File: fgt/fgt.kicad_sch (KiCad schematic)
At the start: 28 parts, among them J1 Conn_01x03, J2 USB_B_Mini, J4 Conn_01x06, SW1 Reset, SW2 SW-, SW3 SW_M/BOOT, SW4 SW+, U1 ESP32-C3-WROOM-02, U3 BMP280, U4 HT75xx-1-SOT89

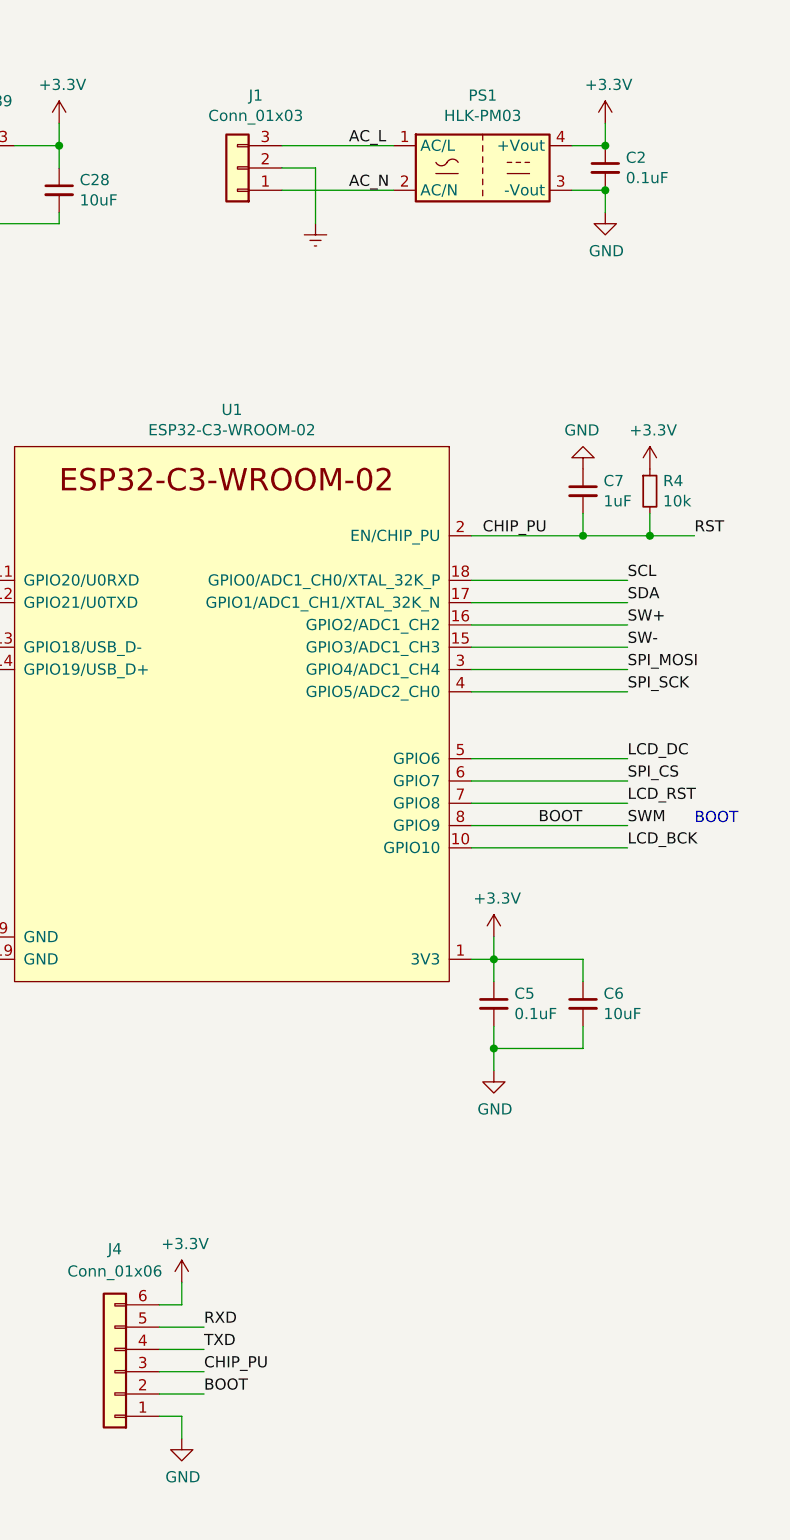
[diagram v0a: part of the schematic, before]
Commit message: placing locating holes
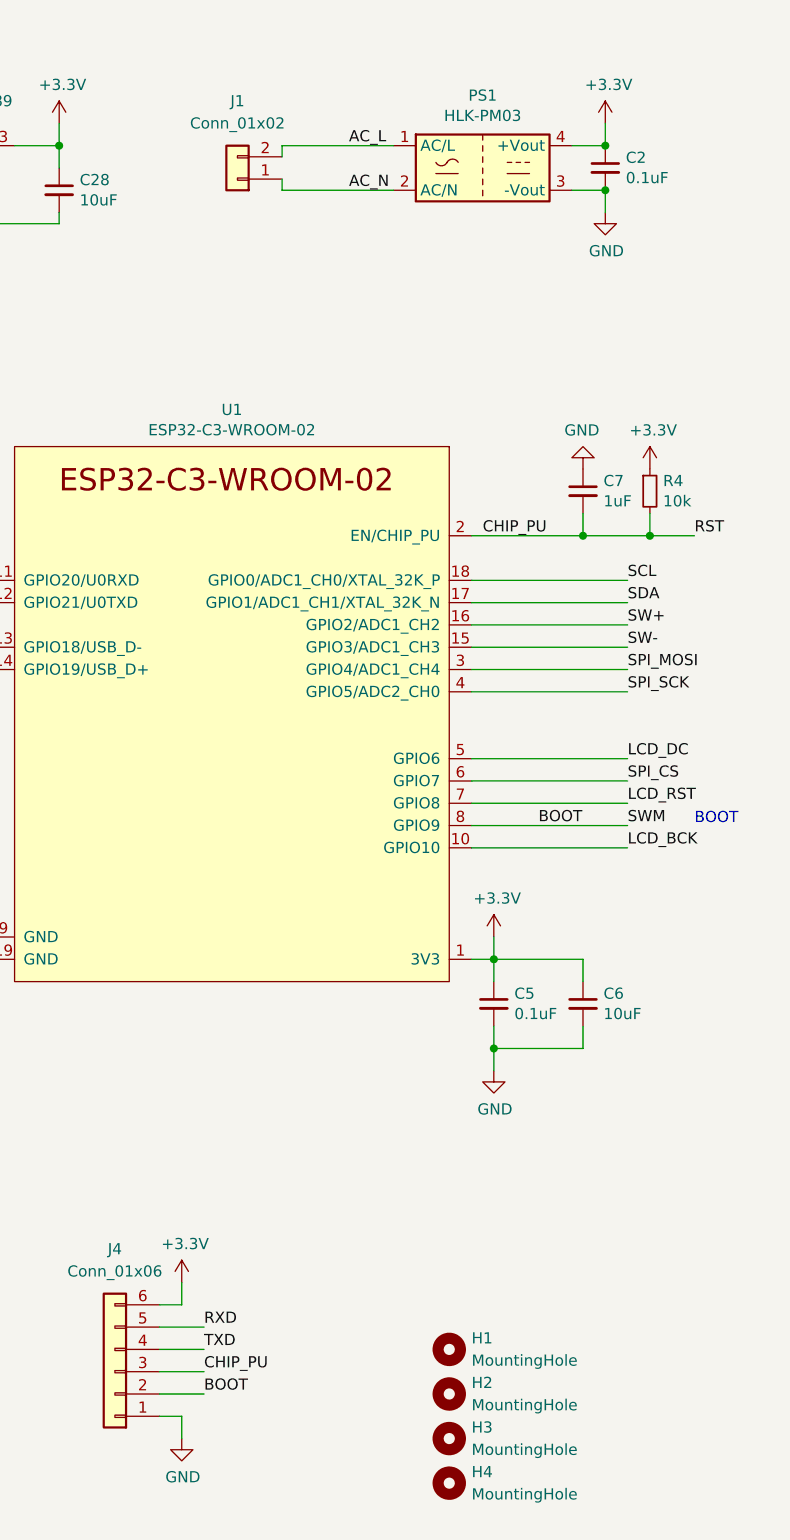
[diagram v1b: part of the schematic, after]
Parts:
- removed J1: Conn_01x03, Connector_Phoenix_MC:PhoenixContact_MCV_1,5_3-G-3.5_1x03_P3.50mm_Vertical, symbol Connector_Generic:Conn_01x03
- added H1, H2, H3, H4: MountingHole, MountingHole:MountingHole_3.2mm_M3_DIN965, symbol Mechanical:MountingHole
- added J1: Conn_01x02, Connector_Phoenix_MSTB:PhoenixContact_MSTBVA_2,5_2-G-5,08_1x02_P5.08mm_Vertical, symbol Connector_Generic:Conn_01x02
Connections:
- net AC_L: now also J1.2 (Pin_2)
- net AC_N: now also J1.1 (Pin_1)
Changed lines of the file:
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@@
   (title_block
     (title "FGT")
-    (date "2021-12-27")
+    (date "2022-01-01")
     (rev "v0.0.0")
     (company "Juraj Giertl")
@@
     (stroke (width 0) (type default) (color 0 0 0 0))
   )
-  (wire (pts (xy 144.78 38.1) (xy 144.78 44.45))
-    (stroke (width 0) (type default) (color 0 0 0 0))
-  )
   (wire (pts (xy 73.66 165.1) (xy 76.2 165.1))
     (stroke (width 0) (type default) (color 0 0 0 0))
@@
     (stroke (width 0) (type default) (color 0 0 0 0))
   )
+  (wire (pts (xy 140.97 39.37) (xy 140.97 40.64))
+    (stroke (width 0) (type default) (color 0 0 0 0))
+  )
   (wire (pts (xy 252.73 129.54) (xy 252.73 130.81))
     (stroke (width 0) (type default) (color 0 0 0 0))
@@
     (stroke (width 0) (type default) (color 0 0 0 0))
   )
-  (wire (pts (xy 140.97 38.1) (xy 144.78 38.1))
+  (wire (pts (xy 140.97 35.56) (xy 140.97 36.83))
     (stroke (width 0) (type default) (color 0 0 0 0))
   )
@@
     (pin "2")
   )
-  (symbol (lib_id "Connector_Generic:Conn_01x03") (at 135.89 38.1 180) (unit 1)
-    (in_bom yes) (on_board yes)
-    (property "Reference" "J1" (id 0) (at 137.9728 29.845 0))
-    (property "Value" "Conn_01x03" (id 1) (at 137.9728 32.1564 0))
-    (property "Footprint" "Connector_Phoenix_MC:PhoenixContact_MCV_1,5_3-G-3.5_1x03_P3.50mm_Vertical" (id 2) (at 135.89 38.1 0)
-      (effects (font (size 1.27 1.27)) hide)
-    )
-    (property "Datasheet" "~" (id 3) (at 135.89 38.1 0)
-      (effects (font (size 1.27 1.27)) hide)
-    )
-    (pin "1")
-    (pin "2")
-    (pin "3")
-  )
   (symbol (lib_id "power:+3.3V") (at 177.8 33.02 0) (unit 1)
     (in_bom yes) (on_board yes)
@@
     )
     (property "Datasheet" "" (id 3) (at 177.8 43.18 0)
-      (effects (font (size 1.27 1.27)) hide)
-    )
-    (pin "1")
-  )
-  (symbol (lib_id "power:Earth") (at 144.78 44.45 0) (unit 1)
-    (in_bom yes) (on_board yes)
-    (property "Reference" "#PWR04" (id 0) (at 144.78 50.8 0)
-      (effects (font (size 1.27 1.27)) hide)
-    )
-    (property "Value" "Earth" (id 1) (at 144.78 48.26 0)
-      (effects (font (size 1.27 1.27)) hide)
-    )
-    (property "Footprint" "" (id 2) (at 144.78 44.45 0)
-      (effects (font (size 1.27 1.27)) hide)
-    )
-    (property "Datasheet" "~" (id 3) (at 144.78 44.45 0)
       (effects (font (size 1.27 1.27)) hide)
     )
@@
     (pin "1")
   )
+  (symbol (lib_id "Mechanical:MountingHole") (at 160.02 187.96 0) (unit 1)
+    (in_bom yes) (on_board yes) (fields_autoplaced)
+    (property "Reference" "H4" (id 0) (at 162.56 186.6899 0)
+      (effects (font (size 1.27 1.27)) (justify left))
+    )
+    (property "Value" "MountingHole" (id 1) (at 162.56 189.2299 0)
+      (effects (font (size 1.27 1.27)) (justify left))
+    )
+    (property "Footprint" "MountingHole:MountingHole_3.2mm_M3_DIN965" (id 2) (at 160.02 187.96 0)
+      (effects (font (size 1.27 1.27)) hide)
+    )
+    (property "Datasheet" "~" (id 3) (at 160.02 187.96 0)
+      (effects (font (size 1.27 1.27)) hide)
+    )
+  )
+  (symbol (lib_id "Mechanical:MountingHole") (at 160.02 182.88 0) (unit 1)
+    (in_bom yes) (on_board yes) (fields_autoplaced)
+    (property "Reference" "H3" (id 0) (at 162.56 181.6099 0)
+      (effects (font (size 1.27 1.27)) (justify left))
+    )
+    (property "Value" "MountingHole" (id 1) (at 162.56 184.1499 0)
+      (effects (font (size 1.27 1.27)) (justify left))
+    )
+    (property "Footprint" "MountingHole:MountingHole_3.2mm_M3_DIN965" (id 2) (at 160.02 182.88 0)
+      (effects (font (size 1.27 1.27)) hide)
+    )
+    (property "Datasheet" "~" (id 3) (at 160.02 182.88 0)
+      (effects (font (size 1.27 1.27)) hide)
+    )
+  )
+  (symbol (lib_id "Connector_Generic:Conn_01x02") (at 135.89 39.37 180) (unit 1)
+    (in_bom yes) (on_board yes) (fields_autoplaced)
+    (property "Reference" "J1" (id 0) (at 135.89 30.48 0))
+    (property "Value" "Conn_01x02" (id 1) (at 135.89 33.02 0))
+    (property "Footprint" "Connector_Phoenix_MSTB:PhoenixContact_MSTBVA_2,5_2-G-5,08_1x02_P5.08mm_Vertical" (id 2) (at 135.89 39.37 0)
+      (effects (font (size 1.27 1.27)) hide)
+    )
+    (property "Datasheet" "~" (id 3) (at 135.89 39.37 0)
+      (effects (font (size 1.27 1.27)) hide)
+    )
+    (pin "1")
+    (pin "2")
+  )
   (symbol (lib_id "Device:C_Small") (at 115.57 40.64 0) (unit 1)
     (in_bom yes) (on_board yes)
@@
     )
     (pin "1")
+  )
+  (symbol (lib_id "Mechanical:MountingHole") (at 160.02 172.72 0) (unit 1)
+    (in_bom yes) (on_board yes) (fields_autoplaced)
+    (property "Reference" "H1" (id 0) (at 162.56 171.4499 0)
+      (effects (font (size 1.27 1.27)) (justify left))
+    )
+    (property "Value" "MountingHole" (id 1) (at 162.56 173.9899 0)
+      (effects (font (size 1.27 1.27)) (justify left))
+    )
+    (property "Footprint" "MountingHole:MountingHole_3.2mm_M3_DIN965" (id 2) (at 160.02 172.72 0)
+      (effects (font (size 1.27 1.27)) hide)
+    )
+    (property "Datasheet" "~" (id 3) (at 160.02 172.72 0)
+      (effects (font (size 1.27 1.27)) hide)
+    )
   )
   (symbol (lib_id "Device:C_Small") (at 88.9 40.64 0) (unit 1)
@@
     (pin "6")
   )
+  (symbol (lib_id "Mechanical:MountingHole") (at 160.02 177.8 0) (unit 1)
+    (in_bom yes) (on_board yes) (fields_autoplaced)
+    (property "Reference" "H2" (id 0) (at 162.56 176.5299 0)
+      (effects (font (size 1.27 1.27)) (justify left))
+    )
+    (property "Value" "MountingHole" (id 1) (at 162.56 179.0699 0)
+      (effects (font (size 1.27 1.27)) (justify left))
+    )
+    (property "Footprint" "MountingHole:MountingHole_3.2mm_M3_DIN965" (id 2) (at 160.02 177.8 0)
+      (effects (font (size 1.27 1.27)) hide)
+    )
+    (property "Datasheet" "~" (id 3) (at 160.02 177.8 0)
+      (effects (font (size 1.27 1.27)) hide)
+    )
+  )
   (sheet (at 242.57 86.36) (size 22.86 17.78) (fields_autoplaced)
     (stroke (width 0) (type solid) (color 0 0 0 0))
@@
       (reference "#PWR03") (unit 1) (value "GND") (footprint "")
     )
-    (path "/00000000-0000-0000-0000-000061c85377"
-      (reference "#PWR04") (unit 1) (value "Earth") (footprint "")
-    )
     (path "/00000000-0000-0000-0000-000061ca0dac"
       (reference "#PWR05") (unit 1) (value "+5V") (footprint "")
@@
       (reference "C28") (unit 1) (value "10uF") (footprint "Capacitor_SMD:C_0805_2012Metric")
     )
-    (path "/00000000-0000-0000-0000-000061c7b75e"
-      (reference "J1") (unit 1) (value "Conn_01x03") (footprint "Connector_Phoenix_MC:PhoenixContact_MCV_1,5_3-G-3.5_1x03_P3.50mm_Vertical")
+    (path "/69ab893d-e72a-4903-8a42-16f6b5eb229b"
+      (reference "H1") (unit 1) (value "MountingHole") (footprint "MountingHole:MountingHole_3.2mm_M3_DIN965")
+    )
+    (path "/fd96f853-b86f-4839-b405-9056fd204602"
+      (reference "H2") (unit 1) (value "MountingHole") (footprint "MountingHole:MountingHole_3.2mm_M3_DIN965")
+    )
+    (path "/2d804580-45d8-4d5b-af99-e9291a298cf1"
+      (reference "H3") (unit 1) (value "MountingHole") (footprint "MountingHole:MountingHole_3.2mm_M3_DIN965")
+    )
+    (path "/187ef78f-31ae-4766-b71e-18f19d93ab5e"
+      (reference "H4") (unit 1) (value "MountingHole") (footprint "MountingHole:MountingHole_3.2mm_M3_DIN965")
+    )
+    (path "/3b73c3cb-5737-490a-aab8-e1dbaa5170c5"
+      (reference "J1") (unit 1) (value "Conn_01x02") (footprint "Connector_Phoenix_MSTB:PhoenixContact_MSTBVA_2,5_2-G-5,08_1x02_P5.08mm_Vertical")
     )
     (path "/00000000-0000-0000-0000-000061c99a05"

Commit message: layout done v1.0.0
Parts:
- added H5, H6: MountingHole, MountingHole:MountingHole_3.2mm_M3_DIN965, symbol Mechanical:MountingHole
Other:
- moved on the sheet: H1, H2, H3, H4
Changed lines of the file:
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@@
     (title "FGT")
     (date "2022-01-01")
-    (rev "v0.0.0")
+    (rev "v1.0.0")
     (company "Juraj Giertl")
     (comment 1 "j74a8g@gmail.com")
@@
     (pin "1")
   )
-  (symbol (lib_id "Mechanical:MountingHole") (at 160.02 187.96 0) (unit 1)
+  (symbol (lib_id "Mechanical:MountingHole") (at 156.21 182.88 0) (unit 1)
     (in_bom yes) (on_board yes) (fields_autoplaced)
-    (property "Reference" "H4" (id 0) (at 162.56 186.6899 0)
-      (effects (font (size 1.27 1.27)) (justify left))
-    )
-    (property "Value" "MountingHole" (id 1) (at 162.56 189.2299 0)
-      (effects (font (size 1.27 1.27)) (justify left))
-    )
-    (property "Footprint" "MountingHole:MountingHole_3.2mm_M3_DIN965" (id 2) (at 160.02 187.96 0)
-      (effects (font (size 1.27 1.27)) hide)
-    )
-    (property "Datasheet" "~" (id 3) (at 160.02 187.96 0)
-      (effects (font (size 1.27 1.27)) hide)
-    )
-  )
-  (symbol (lib_id "Mechanical:MountingHole") (at 160.02 182.88 0) (unit 1)
+    (property "Reference" "H4" (id 0) (at 158.75 181.6099 0)
+      (effects (font (size 1.27 1.27)) (justify left))
+    )
+    (property "Value" "MountingHole" (id 1) (at 158.75 184.1499 0)
+      (effects (font (size 1.27 1.27)) (justify left))
+    )
+    (property "Footprint" "MountingHole:MountingHole_3.2mm_M3_DIN965" (id 2) (at 156.21 182.88 0)
+      (effects (font (size 1.27 1.27)) hide)
+    )
+    (property "Datasheet" "~" (id 3) (at 156.21 182.88 0)
+      (effects (font (size 1.27 1.27)) hide)
+    )
+  )
+  (symbol (lib_id "Mechanical:MountingHole") (at 156.21 193.04 0) (unit 1)
     (in_bom yes) (on_board yes) (fields_autoplaced)
-    (property "Reference" "H3" (id 0) (at 162.56 181.6099 0)
-      (effects (font (size 1.27 1.27)) (justify left))
-    )
-    (property "Value" "MountingHole" (id 1) (at 162.56 184.1499 0)
-      (effects (font (size 1.27 1.27)) (justify left))
-    )
-    (property "Footprint" "MountingHole:MountingHole_3.2mm_M3_DIN965" (id 2) (at 160.02 182.88 0)
-      (effects (font (size 1.27 1.27)) hide)
-    )
-    (property "Datasheet" "~" (id 3) (at 160.02 182.88 0)
+    (property "Reference" "H6" (id 0) (at 158.75 191.7699 0)
+      (effects (font (size 1.27 1.27)) (justify left))
+    )
+    (property "Value" "MountingHole" (id 1) (at 158.75 194.3099 0)
+      (effects (font (size 1.27 1.27)) (justify left))
+    )
+    (property "Footprint" "MountingHole:MountingHole_3.2mm_M3_DIN965" (id 2) (at 156.21 193.04 0)
+      (effects (font (size 1.27 1.27)) hide)
+    )
+    (property "Datasheet" "~" (id 3) (at 156.21 193.04 0)
+      (effects (font (size 1.27 1.27)) hide)
+    )
+  )
+  (symbol (lib_id "Mechanical:MountingHole") (at 156.21 177.8 0) (unit 1)
+    (in_bom yes) (on_board yes) (fields_autoplaced)
+    (property "Reference" "H3" (id 0) (at 158.75 176.5299 0)
+      (effects (font (size 1.27 1.27)) (justify left))
+    )
+    (property "Value" "MountingHole" (id 1) (at 158.75 179.0699 0)
+      (effects (font (size 1.27 1.27)) (justify left))
+    )
+    (property "Footprint" "MountingHole:MountingHole_3.2mm_M3_DIN965" (id 2) (at 156.21 177.8 0)
+      (effects (font (size 1.27 1.27)) hide)
+    )
+    (property "Datasheet" "~" (id 3) (at 156.21 177.8 0)
       (effects (font (size 1.27 1.27)) hide)
     )
@@
     (pin "1")
   )
-  (symbol (lib_id "Mechanical:MountingHole") (at 160.02 172.72 0) (unit 1)
+  (symbol (lib_id "Mechanical:MountingHole") (at 156.21 187.96 0) (unit 1)
     (in_bom yes) (on_board yes) (fields_autoplaced)
-    (property "Reference" "H1" (id 0) (at 162.56 171.4499 0)
-      (effects (font (size 1.27 1.27)) (justify left))
-    )
-    (property "Value" "MountingHole" (id 1) (at 162.56 173.9899 0)
-      (effects (font (size 1.27 1.27)) (justify left))
-    )
-    (property "Footprint" "MountingHole:MountingHole_3.2mm_M3_DIN965" (id 2) (at 160.02 172.72 0)
-      (effects (font (size 1.27 1.27)) hide)
-    )
-    (property "Datasheet" "~" (id 3) (at 160.02 172.72 0)
+    (property "Reference" "H5" (id 0) (at 158.75 186.6899 0)
+      (effects (font (size 1.27 1.27)) (justify left))
+    )
+    (property "Value" "MountingHole" (id 1) (at 158.75 189.2299 0)
+      (effects (font (size 1.27 1.27)) (justify left))
+    )
+    (property "Footprint" "MountingHole:MountingHole_3.2mm_M3_DIN965" (id 2) (at 156.21 187.96 0)
+      (effects (font (size 1.27 1.27)) hide)
+    )
+    (property "Datasheet" "~" (id 3) (at 156.21 187.96 0)
+      (effects (font (size 1.27 1.27)) hide)
+    )
+  )
+  (symbol (lib_id "Mechanical:MountingHole") (at 156.21 167.64 0) (unit 1)
+    (in_bom yes) (on_board yes) (fields_autoplaced)
+    (property "Reference" "H1" (id 0) (at 158.75 166.3699 0)
+      (effects (font (size 1.27 1.27)) (justify left))
+    )
+    (property "Value" "MountingHole" (id 1) (at 158.75 168.9099 0)
+      (effects (font (size 1.27 1.27)) (justify left))
+    )
+    (property "Footprint" "MountingHole:MountingHole_3.2mm_M3_DIN965" (id 2) (at 156.21 167.64 0)
+      (effects (font (size 1.27 1.27)) hide)
+    )
+    (property "Datasheet" "~" (id 3) (at 156.21 167.64 0)
       (effects (font (size 1.27 1.27)) hide)
     )
@@
     (pin "6")
   )
-  (symbol (lib_id "Mechanical:MountingHole") (at 160.02 177.8 0) (unit 1)
+  (symbol (lib_id "Mechanical:MountingHole") (at 156.21 172.72 0) (unit 1)
     (in_bom yes) (on_board yes) (fields_autoplaced)
-    (property "Reference" "H2" (id 0) (at 162.56 176.5299 0)
-      (effects (font (size 1.27 1.27)) (justify left))
-    )
-    (property "Value" "MountingHole" (id 1) (at 162.56 179.0699 0)
-      (effects (font (size 1.27 1.27)) (justify left))
-    )
-    (property "Footprint" "MountingHole:MountingHole_3.2mm_M3_DIN965" (id 2) (at 160.02 177.8 0)
-      (effects (font (size 1.27 1.27)) hide)
-    )
-    (property "Datasheet" "~" (id 3) (at 160.02 177.8 0)
+    (property "Reference" "H2" (id 0) (at 158.75 171.4499 0)
+      (effects (font (size 1.27 1.27)) (justify left))
+    )
+    (property "Value" "MountingHole" (id 1) (at 158.75 173.9899 0)
+      (effects (font (size 1.27 1.27)) (justify left))
+    )
+    (property "Footprint" "MountingHole:MountingHole_3.2mm_M3_DIN965" (id 2) (at 156.21 172.72 0)
+      (effects (font (size 1.27 1.27)) hide)
+    )
+    (property "Datasheet" "~" (id 3) (at 156.21 172.72 0)
       (effects (font (size 1.27 1.27)) hide)
     )
@@
       (reference "H4") (unit 1) (value "MountingHole") (footprint "MountingHole:MountingHole_3.2mm_M3_DIN965")
     )
+    (path "/5f9d1197-9ec6-491c-9694-c6bf1e4363ce"
+      (reference "H5") (unit 1) (value "MountingHole") (footprint "MountingHole:MountingHole_3.2mm_M3_DIN965")
+    )
+    (path "/19a40444-388b-4bba-b767-0f02a6e7ab7f"
+      (reference "H6") (unit 1) (value "MountingHole") (footprint "MountingHole:MountingHole_3.2mm_M3_DIN965")
+    )
     (path "/3b73c3cb-5737-490a-aab8-e1dbaa5170c5"

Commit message: DRC done
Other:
- title: FGT -> ${TITLE}
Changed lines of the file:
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@@
   (paper "A4")
   (title_block
-    (title "FGT")
-    (date "2022-01-04")
-    (rev "v1.1.0")
+    (title "${TITLE}")
+    (date "${DATE}")
+    (rev "${REVISION}")
     (company "Juraj Giertl")
     (comment 1 "j74a8g@gmail.com")
